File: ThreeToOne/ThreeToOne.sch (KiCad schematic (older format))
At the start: 216 parts, among them SW1 Switch, SW10 Switch, SW100 Switch, SW101 Switch, SW11 Switch, SW12 Switch, SW13 Switch, SW14 Switch, SW15 Switch, SW16 Switch, SW17 REsw, SW18 Switch, SW19 Switch, SW2 Switch, SW20 Switch, SW21 Switch, SW22 Switch, SW23 Switch, SW24 Switch, SW25 Switch, SW26 Switch, SW27 Switch, SW28 Switch, SW29 Switch, SW3 Switch, SW30 Switch, SW31 Switch, SW32 Switch, SW33 Switch, SW34 Switch, SW35 Switch, SW36 Switch, SW37 Switch, SW38 Switch, SW39 Switch, SW4 Switch, SW40 Switch, SW41 Switch, SW42 Switch, SW43 Switch, SW44 Switch, SW45 Switch, SW46 Switch, SW47 Switch, SW48 Switch, SW49 Switch, SW5 Switch, SW50 Switch, SW51 Switch, SW52 Switch, SW53 Switch, SW54 Switch, SW55 Switch, SW56 Switch, SW57 Switch, SW58 Switch, SW59 Switch, SW6 Switch, SW60 Switch, SW61 Switch, SW62 Switch, SW63 Switch, SW64 Switch, SW65 Switch, SW66 Switch, SW67 Switch, SW68 Switch, SW69 Switch, SW7 Switch, SW70 Switch, SW71 Switch, SW72 Switch, SW73 Switch, SW74 Switch, SW75 Switch, SW76 Switch, SW77 Switch, SW78 Switch, SW79 Switch, SW8 Switch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

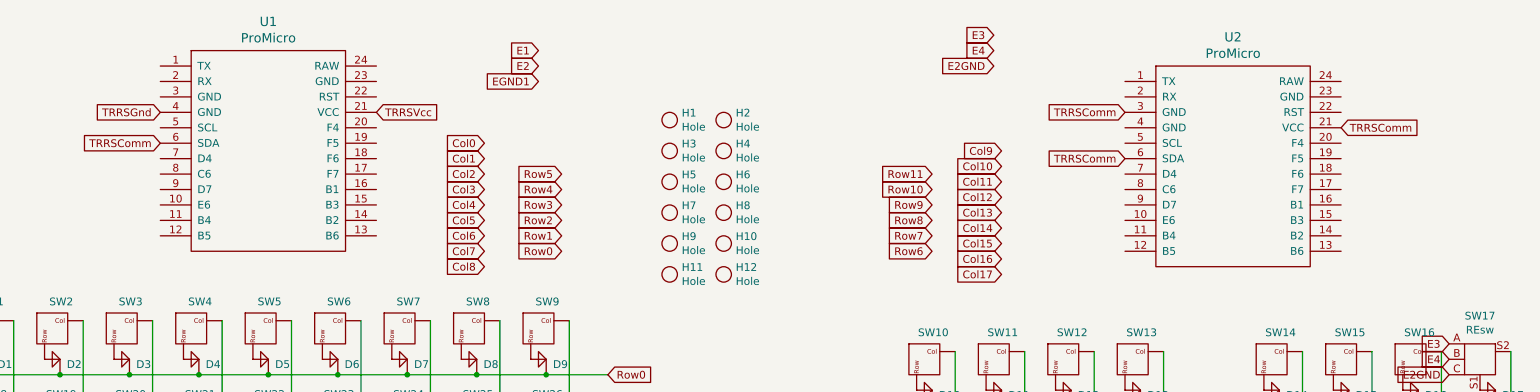
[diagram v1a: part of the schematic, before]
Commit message: Wired all of left half and some of right
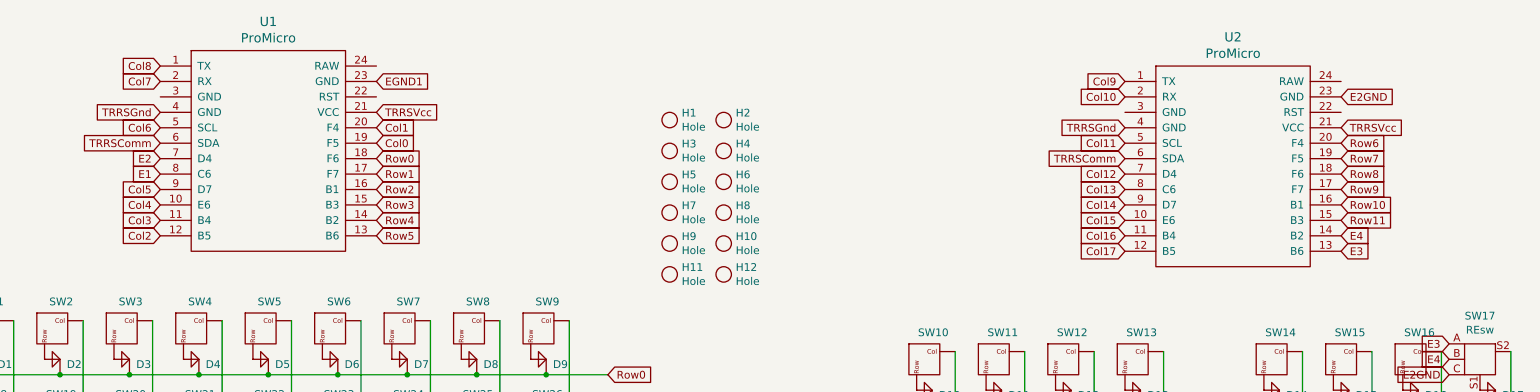
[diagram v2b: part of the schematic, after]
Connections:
- net Col0: now also U1.19 (F5)
- net Col1: now also U1.20 (F4)
- net Col10: now also U2.2 (RX)
- net Col11: now also U2.5 (SCL)
- net Col12: now also U2.7 (D4)
- net Col13: now also U2.8 (C6)
- net Col14: now also U2.9 (D7)
- net Col15: now also U2.10 (E6)
- net Col16: now also U2.11 (B4)
- net Col17: now also U2.12 (B5)
- net Col2: now also U1.12 (B5)
- net Col3: now also U1.11 (B4)
- net Col4: now also U1.10 (E6)
- net Col5: now also U1.9 (D7)
- net Col6: now also U1.5 (SCL)
- net Col7: now also U1.2 (RX)
- net Col8: now also U1.1 (TX)
- net Col9: now also U2.1 (TX)
- net E1: now also U1.8 (C6)
- net E2: now also U1.7 (D4)
- net E2GND: now also U2.23 (GND)
- net E3: now also U2.13 (B6)
- net E4: now also U2.14 (B2)
- net EGND1: now also U1.23 (GND)
- net Row0: now also U1.18 (F6)
- net Row1: now also U1.17 (F7)
- net Row10: now also U2.16 (B1)
- net Row11: now also U2.15 (B3)
- net Row2: now also U1.16 (B1)
- net Row3: now also U1.15 (B3)
- net Row4: now also U1.14 (B2)
- net Row5: now also U1.13 (B6)
- net Row6: now also U2.20 (F4)
- net Row7: now also U2.19 (F5)
- net Row8: now also U2.18 (F6)
- net Row9: now also U2.17 (F7)
- net TRRSComm: no longer U2.21 (VCC), U2.3 (GND)
- net TRRSGnd: now also U2.4 (GND)
- net TRRSVcc: now also U2.21 (VCC)
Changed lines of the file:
@@
 Text GLabel 2000 1100 0    50   Input ~ 0
 TRRSGnd
-Text GLabel 8250 1100 0    50   Input ~ 0
-TRRSComm
 Text GLabel 3400 1100 2    50   Input ~ 0
 TRRSVcc
-Text GLabel 9650 1200 2    50   Input ~ 0
-TRRSComm
-Text GLabel 4450 700  0    50   Input ~ 0
+Text GLabel 2000 1500 0    50   Input ~ 0
 E1
-Text GLabel 4450 800  0    50   Input ~ 0
+Text GLabel 2000 1400 0    50   Input ~ 0
 E2
-Text GLabel 4450 900  0    50   Input ~ 0
+Text GLabel 3400 900  2    50   Input ~ 0
 EGND1
 Connection ~ 4200 5350
@@
 Text GLabel 1050 5900 0    50   Input ~ 0
 Col0
-Text GLabel 4100 1300 0    50   Input ~ 0
+Text GLabel 3400 1300 2    50   Input ~ 0
 Col0
-Text GLabel 4100 1400 0    50   Input ~ 0
+Text GLabel 3400 1200 2    50   Input ~ 0
 Col1
-Text GLabel 4100 1500 0    50   Input ~ 0
+Text GLabel 2000 1900 0    50   Input ~ 0
 Col2
-Text GLabel 4100 1600 0    50   Input ~ 0
+Text GLabel 2000 1800 0    50   Input ~ 0
 Col3
-Text GLabel 4100 1700 0    50   Input ~ 0
+Text GLabel 2000 1700 0    50   Input ~ 0
 Col4
-Text GLabel 4100 1800 0    50   Input ~ 0
+Text GLabel 2000 1600 0    50   Input ~ 0
 Col5
-Text GLabel 4100 1900 0    50   Input ~ 0
+Text GLabel 2000 1200 0    50   Input ~ 0
 Col6
-Text GLabel 4100 2000 0    50   Input ~ 0
+Text GLabel 2000 900  0    50   Input ~ 0
 Col7
-Text GLabel 4100 2100 0    50   Input ~ 0
+Text GLabel 2000 800  0    50   Input ~ 0
 Col8
-Text GLabel 7450 1350 0    50   Input ~ 0
+Text GLabel 8250 900  0    50   Input ~ 0
 Col9
-Text GLabel 7450 1450 0    50   Input ~ 0
+Text GLabel 8250 1000 0    50   Input ~ 0
 Col10
-Text GLabel 7450 1550 0    50   Input ~ 0
+Text GLabel 8250 1300 0    50   Input ~ 0
 Col11
-Text GLabel 7450 1650 0    50   Input ~ 0
+Text GLabel 8250 1500 0    50   Input ~ 0
 Col12
-Text GLabel 7450 1750 0    50   Input ~ 0
+Text GLabel 8250 1600 0    50   Input ~ 0
 Col13
-Text GLabel 7450 1850 0    50   Input ~ 0
+Text GLabel 8250 1700 0    50   Input ~ 0
 Col14
-Text GLabel 7450 1950 0    50   Input ~ 0
+Text GLabel 8250 1800 0    50   Input ~ 0
 Col15
-Text GLabel 7450 2050 0    50   Input ~ 0
+Text GLabel 8250 1900 0    50   Input ~ 0
 Col16
-Text GLabel 7450 2150 0    50   Input ~ 0
+Text GLabel 8250 2000 0    50   Input ~ 0
 Col17
 Text GLabel 6600 5900 0    50   Input ~ 0
@@
 Text GLabel 6600 3000 0    50   Input ~ 0
 Row6
-Text GLabel 4600 2000 0    50   Input ~ 0
+Text GLabel 3400 1400 2    50   Input ~ 0
 Row0
-Text GLabel 4600 1900 0    50   Input ~ 0
+Text GLabel 3400 1500 2    50   Input ~ 0
 Row1
-Text GLabel 4600 1800 0    50   Input ~ 0
+Text GLabel 3400 1600 2    50   Input ~ 0
 Row2
-Text GLabel 4600 1700 0    50   Input ~ 0
+Text GLabel 3400 1700 2    50   Input ~ 0
 Row3
-Text GLabel 4600 1500 0    50   Input ~ 0
+Text GLabel 3400 1900 2    50   Input ~ 0
 Row5
-Text GLabel 4600 1600 0    50   Input ~ 0
+Text GLabel 3400 1800 2    50   Input ~ 0
 Row4
-Text GLabel 7000 1500 0    50   Input ~ 0
+Text GLabel 9650 1800 2    50   Input ~ 0
 Row11
-Text GLabel 7000 1600 0    50   Input ~ 0
+Text GLabel 9650 1700 2    50   Input ~ 0
 Row10
-Text GLabel 7000 1700 0    50   Input ~ 0
+Text GLabel 9650 1600 2    50   Input ~ 0
 Row9
-Text GLabel 7000 1800 0    50   Input ~ 0
+Text GLabel 9650 1500 2    50   Input ~ 0
 Row8
-Text GLabel 7000 1900 0    50   Input ~ 0
+Text GLabel 9650 1400 2    50   Input ~ 0
 Row7
-Text GLabel 7000 2000 0    50   Input ~ 0
+Text GLabel 9650 1300 2    50   Input ~ 0
 Row6
-Text GLabel 7400 600  0    50   Input ~ 0
+Text GLabel 9650 2000 2    50   Input ~ 0
 E3
-Text GLabel 7400 700  0    50   Input ~ 0
+Text GLabel 9650 1900 2    50   Input ~ 0
 E4
-Text GLabel 7400 800  0    50   Input ~ 0
+Text GLabel 9650 1000 2    50   Input ~ 0
 E2GND
 $Comp
@@
 	1    0    0    -1
 $EndComp
+Text GLabel 8250 1200 0    50   Input ~ 0
+TRRSGnd
+Text GLabel 9650 1200 2    50   Input ~ 0
+TRRSVcc
 $EndSCHEMATC

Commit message: Finished + gerbers
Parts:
- removed H1, H10, H11, H12, H2, H3, H4, H5, H6, H7, H8, H9: Hole, KeyboardFootprints:Hole_2mm, symbol KeyboardLibrary:Hole
- removed U2: ProMicro, KeyboardFootprints:ProMicro, symbol KeyboardLibrary:ProMicro
- added LED0, LED1: Diode, KeyboardFootprints:Diode, symbol KeyboardLibrary:Diode
- added R0, R1: Resistor, KeyboardFootprints:Resistor, symbol KeyboardLibrary:Resistor
- added U2: Elite-C, Keebio-Parts:Elite-C, symbol keebio:Elite-C
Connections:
- net Col10: now also U2.2 (RX1/PD2)
- net Col11: now also U2.5 (2/PD1)
- net Col12: now also U2.7 (4/PD4)
- net Col13: now also U2.8 (5/PC6)
- net Col14: now also U2.9 (6/PD7)
- net Col15: now also U2.10 (7/PE6)
- net Col16: now also U2.11 (8/PB4)
- net Col17: now also U2.12 (9/PB5)
- net Col9: now also U2.1 (TX0/PD3)
- net E2GND: now also R0.1, R1.1, U2.23 (GND)
- net E3: now also U2.25 (B7)
- net E4: now also U2.26 (D5)
- net Row10: now also U2.17 (A0/PF7)
- net Row11: now also U2.18 (A1/PF6)
- net Row6: now also U2.20 (A3/PF4)
- net Row7: now also U2.19 (A2/PF5)
- net Row8: now also U2.15 (14/PB3)
- net Row9: now also U2.16 (15/PB1)
- net TRRSComm: now also U2.6 (3/PD0)
- net TRRSGnd: now also U2.4 (GND)
- net TRRSVcc: now also U2.21 (VCC)
- new net: LED1.1 (K), U2.13 (10/PB6)
- new net: LED0.1 (K), U2.14 (16/PB2)
- new net: LED0.2 (A), R0.2
- new net: LED1.2 (A), R1.2
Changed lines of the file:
@@
-	1    0    0    -1
-$EndComp
-$Comp
-L KeyboardLibrary:ProMicro U2
-U 1 1 607B0D82
-P 8950 1650
-F 0 "U2" H 8950 2687 60  0000 C CNN
-F 1 "ProMicro" H 8950 2581 60  0000 C CNN
-F 2 "KeyboardFootprints:ProMicro" H 9050 600 60  0001 C CNN
-F 3 "" H 9050 600 60  0000 C CNN
-	1    8950 1650
 	1    0    0    -1
 $EndComp
@@
 Text GLabel 10350 2800 0    50   Input ~ 0
 E2GND
-Text GLabel 8250 1400 0    50   Input ~ 0
+Text GLabel 8200 1400 0    50   Input ~ 0
 TRRSComm
 Text GLabel 2000 1300 0    50   Input ~ 0
@@
 Text GLabel 2000 800  0    50   Input ~ 0
 Col8
-Text GLabel 8250 900  0    50   Input ~ 0
+Text GLabel 8200 900  0    50   Input ~ 0
 Col9
-Text GLabel 8250 1000 0    50   Input ~ 0
+Text GLabel 8200 1000 0    50   Input ~ 0
 Col10
-Text GLabel 8250 1300 0    50   Input ~ 0
+Text GLabel 8200 1300 0    50   Input ~ 0
 Col11
-Text GLabel 8250 1500 0    50   Input ~ 0
+Text GLabel 8200 1500 0    50   Input ~ 0
 Col12
-Text GLabel 8250 1600 0    50   Input ~ 0
+Text GLabel 8200 1600 0    50   Input ~ 0
 Col13
-Text GLabel 8250 1700 0    50   Input ~ 0
+Text GLabel 8200 1700 0    50   Input ~ 0
 Col14
-Text GLabel 8250 1800 0    50   Input ~ 0
+Text GLabel 8200 1800 0    50   Input ~ 0
 Col15
-Text GLabel 8250 1900 0    50   Input ~ 0
+Text GLabel 8200 1900 0    50   Input ~ 0
 Col16
-Text GLabel 8250 2000 0    50   Input ~ 0
+Text GLabel 8200 2000 0    50   Input ~ 0
 Col17
 Text GLabel 6600 5900 0    50   Input ~ 0
@@
 Text GLabel 3400 1800 2    50   Input ~ 0
 Row4
-Text GLabel 9650 1800 2    50   Input ~ 0
-Row11
-Text GLabel 9650 1700 2    50   Input ~ 0
-Row10
-Text GLabel 9650 1600 2    50   Input ~ 0
-Row9
-Text GLabel 9650 1500 2    50   Input ~ 0
-Row8
-Text GLabel 9650 1400 2    50   Input ~ 0
-Row7
-Text GLabel 9650 1300 2    50   Input ~ 0
-Row6
-Text GLabel 9650 2000 2    50   Input ~ 0
+Text GLabel 8700 2400 3    50   Input ~ 0
 E3
-Text GLabel 9650 1900 2    50   Input ~ 0
+Text GLabel 8800 2400 3    50   Input ~ 0
 E4
-Text GLabel 9650 1000 2    50   Input ~ 0
-E2GND
-$Comp
-L KeyboardLibrary:Hole H1
-U 1 1 604DCAA4
-P 5300 1150
-F 0 "H1" H 5378 1196 50  0000 L CNN
-F 1 "Hole" H 5378 1105 50  0000 L CNN
-F 2 "KeyboardFootprints:Hole_2mm" H 5300 1100 50  0001 C CNN
-F 3 "" H 5300 1100 50  0001 C CNN
-	1    5300 1150
-	1    0    0    -1
-$EndComp
-$Comp
-L KeyboardLibrary:Hole H3
-U 1 1 604DF4A1
-P 5300 1350
-F 0 "H3" H 5378 1396 50  0000 L CNN
-F 1 "Hole" H 5378 1305 50  0000 L CNN
-F 2 "KeyboardFootprints:Hole_2mm" H 5300 1300 50  0001 C CNN
-F 3 "" H 5300 1300 50  0001 C CNN
-	1    5300 1350
-	1    0    0    -1
-$EndComp
-$Comp
-L KeyboardLibrary:Hole H5
-U 1 1 604EAA4A
-P 5300 1550
-F 0 "H5" H 5378 1596 50  0000 L CNN
-F 1 "Hole" H 5378 1505 50  0000 L CNN
-F 2 "KeyboardFootprints:Hole_2mm" H 5300 1500 50  0001 C CNN
-F 3 "" H 5300 1500 50  0001 C CNN
-	1    5300 1550
-	1    0    0    -1
-$EndComp
-$Comp
-L KeyboardLibrary:Hole H2
-U 1 1 604F6F10
-P 5650 1150
-F 0 "H2" H 5728 1196 50  0000 L CNN
-F 1 "Hole" H 5728 1105 50  0000 L CNN
-F 2 "KeyboardFootprints:Hole_2mm" H 5650 1100 50  0001 C CNN
-F 3 "" H 5650 1100 50  0001 C CNN
-	1    5650 1150
-	1    0    0    -1
-$EndComp
-$Comp
-L KeyboardLibrary:Hole H4
-U 1 1 604F6F16
-P 5650 1350
-F 0 "H4" H 5728 1396 50  0000 L CNN
-F 1 "Hole" H 5728 1305 50  0000 L CNN
-F 2 "KeyboardFootprints:Hole_2mm" H 5650 1300 50  0001 C CNN
-F 3 "" H 5650 1300 50  0001 C CNN
-	1    5650 1350
-	1    0    0    -1
-$EndComp
-$Comp
-L KeyboardLibrary:Hole H6
-U 1 1 604F6F1C
-P 5650 1550
-F 0 "H6" H 5728 1596 50  0000 L CNN
-F 1 "Hole" H 5728 1505 50  0000 L CNN
-F 2 "KeyboardFootprints:Hole_2mm" H 5650 1500 50  0001 C CNN
-F 3 "" H 5650 1500 50  0001 C CNN
-	1    5650 1550
-	1    0    0    -1
-$EndComp
-$Comp
-L KeyboardLibrary:Hole H8
-U 1 1 60502740
-P 5650 1750
-F 0 "H8" H 5728 1796 50  0000 L CNN
-F 1 "Hole" H 5728 1705 50  0000 L CNN
-F 2 "KeyboardFootprints:Hole_2mm" H 5650 1700 50  0001 C CNN
-F 3 "" H 5650 1700 50  0001 C CNN
-	1    5650 1750
-	1    0    0    -1
-$EndComp
-$Comp
-L KeyboardLibrary:Hole H10
-U 1 1 60502746
-P 5650 1950
-F 0 "H10" H 5728 1996 50  0000 L CNN
-F 1 "Hole" H 5728 1905 50  0000 L CNN
-F 2 "KeyboardFootprints:Hole_2mm" H 5650 1900 50  0001 C CNN
-F 3 "" H 5650 1900 50  0001 C CNN
-	1    5650 1950
-	1    0    0    -1
-$EndComp
-$Comp
-L KeyboardLibrary:Hole H12
-U 1 1 6050274C
-P 5650 2150
-F 0 "H12" H 5728 2196 50  0000 L CNN
-F 1 "Hole" H 5728 2105 50  0000 L CNN
-F 2 "KeyboardFootprints:Hole_2mm" H 5650 2100 50  0001 C CNN
-F 3 "" H 5650 2100 50  0001 C CNN
-	1    5650 2150
-	1    0    0    -1
-$EndComp
-$Comp
-L KeyboardLibrary:Hole H7
-U 1 1 6050DD66
-P 5300 1750
-F 0 "H7" H 5378 1796 50  0000 L CNN
-F 1 "Hole" H 5378 1705 50  0000 L CNN
-F 2 "KeyboardFootprints:Hole_2mm" H 5300 1700 50  0001 C CNN
-F 3 "" H 5300 1700 50  0001 C CNN
-	1    5300 1750
-	1    0    0    -1
-$EndComp
-$Comp
-L KeyboardLibrary:Hole H9
-U 1 1 6050DD6C
-P 5300 1950
-F 0 "H9" H 5378 1996 50  0000 L CNN
-F 1 "Hole" H 5378 1905 50  0000 L CNN
-F 2 "KeyboardFootprints:Hole_2mm" H 5300 1900 50  0001 C CNN
-F 3 "" H 5300 1900 50  0001 C CNN
-	1    5300 1950
-	1    0    0    -1
-$EndComp
-$Comp
-L KeyboardLibrary:Hole H11
-U 1 1 6050DD72
-P 5300 2150
-F 0 "H11" H 5378 2196 50  0000 L CNN
-F 1 "Hole" H 5378 2105 50  0000 L CNN
-F 2 "KeyboardFootprints:Hole_2mm" H 5300 2100 50  0001 C CNN
-F 3 "" H 5300 2100 50  0001 C CNN
-	1    5300 2150
-	1    0    0    -1
-$EndComp
 Wire Wire Line
 	2250 3950 2700 3950
@@
 	1    0    0    -1
 $EndComp
-Text GLabel 8250 1200 0    50   Input ~ 0
+Text GLabel 8200 1200 0    50   Input ~ 0
 TRRSGnd
-Text GLabel 9650 1200 2    50   Input ~ 0
+$Comp
+L keebio:Elite-C U2
+U 1 1 6055E9BB
+P 8900 1450
+F 0 "U2" H 8900 2287 60  0000 C CNN
+F 1 "Elite-C" H 8900 2181 60  0000 C CNN
+F 2 "Keebio-Parts:Elite-C" V 9950 -1050 60  0001 C CNN
+F 3 "" V 9950 -1050 60  0001 C CNN
+	1    8900 1450
+	1    0    0    -1
+$EndComp
+Text GLabel 9600 1200 2    50   Input ~ 0
 TRRSVcc
+Text GLabel 9850 1000 2    50   Input ~ 0
+E2GND
+Text GLabel 9600 1300 2    50   Input ~ 0
+Row6
+Text GLabel 9600 1400 2    50   Input ~ 0
+Row7
+Text GLabel 9600 1800 2    50   Input ~ 0
+Row8
+Text GLabel 9600 1700 2    50   Input ~ 0
+Row9
+Text GLabel 9600 1600 2    50   Input ~ 0
+Row10
+Text GLabel 9600 1500 2    50   Input ~ 0
+Row11
+$Comp
+L KeyboardLibrary:Diode LED0
+U 1 1 606358A6
+P 9800 1900
+F 0 "LED0" H 9944 1867 50  0000 L CNN
+F 1 "Diode" H 9900 2000 50  0001 C CNN
+F 2 "KeyboardFootprints:Diode" H 9900 2000 50  0001 C CNN
+F 3 "" H 9900 2000 50  0001 C CNN
+	1    9800 1900
+	1    0    0    -1
+$EndComp
+$Comp
+L KeyboardLibrary:Diode LED1
+U 1 1 60637F62
+P 9600 2000
+F 0 "LED1" H 9744 1967 50  0000 L CNN
+F 1 "Diode" H 9700 2100 50  0001 C CNN
+F 2 "KeyboardFootprints:Diode" H 9700 2100 50  0001 C CNN
+F 3 "" H 9700 2100 50  0001 C CNN
+	1    9600 2000
+	1    0    0    -1
+$EndComp
+Wire Wire Line
+	9600 1900 9800 1900
+Wire Wire Line
+	9800 1000 9800 1100
+Wire Wire Line
+	9800 1100 10200 1100
+Wire Wire Line
+	9600 1000 9800 1000
+Connection ~ 9800 1000
+Wire Wire Line
+	9800 1000 9850 1000
+$Comp
+L KeyboardLibrary:Resistor R0
+U 1 1 6065EAE1
+P 10050 2000
+F 0 "R0" H 10050 1877 50  0000 C CNN
+F 1 "Resistor" H 10050 2000 50  0001 C CNN
+F 2 "KeyboardFootprints:Resistor" H 10050 2000 50  0001 C CNN
+F 3 "" H 10050 2000 50  0001 C CNN
+	1    10050 2000
+	-1   0    0    1
+$EndComp
+$Comp
+L KeyboardLibrary:Resistor R1
+U 1 1 6067AA95
+P 9850 2100
+F 0 "R1" H 9850 1977 50  0000 C CNN
+F 1 "Resistor" H 9850 2100 50  0001 C CNN
+F 2 "KeyboardFootprints:Resistor" H 9850 2100 50  0001 C CNN
+F 3 "" H 9850 2100 50  0001 C CNN
+	1    9850 2100
+	-1   0    0    1
+$EndComp
+Wire Wire Line
+	10000 2100 10200 2100
+Wire Wire Line
+	10200 2100 10200 2000
+Wire Wire Line
+	10200 2000 10200 1100
+Connection ~ 10200 2000
 $EndSCHEMATC

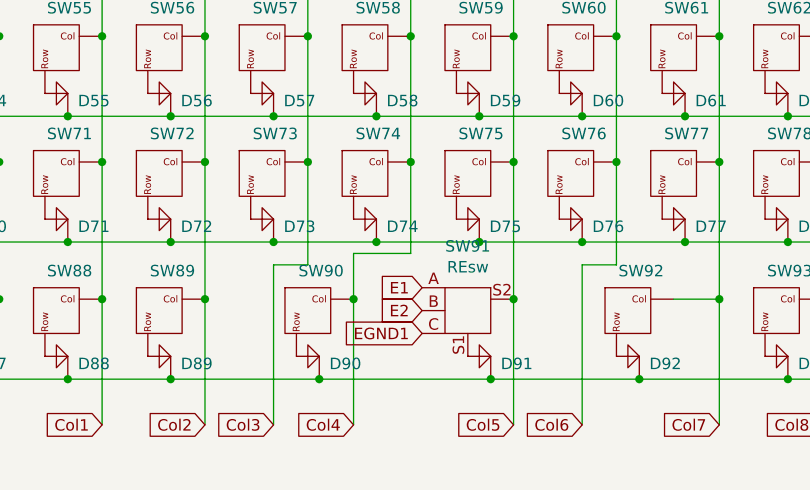
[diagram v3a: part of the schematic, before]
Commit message: moved enc to the left
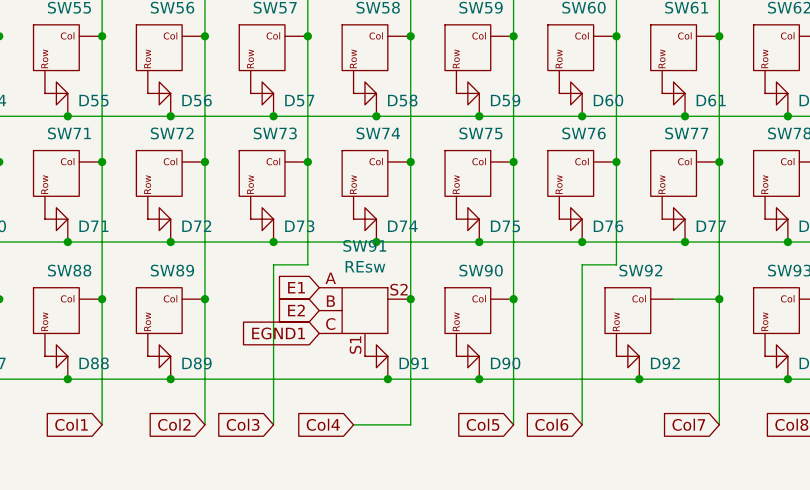
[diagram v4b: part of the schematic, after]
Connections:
- net Col4: now also SW91.S2; no longer SW90.1
- net Col5: now also SW90.1; no longer SW91.S2
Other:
- moved on the sheet: D90, D91, SW90, SW91
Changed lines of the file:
@@
 L KeyboardLibrary:Switch SW90
 U 1 1 60535E84
-P 2500 5500
-F 0 "SW90" H 2458 5773 50  0000 C CNN
-F 1 "Switch" H 2450 5550 50  0001 C CNN
-F 2 "KeyboardFootprints:MX_Choc_Symmetric" H 2500 5500 50  0001 C CNN
-F 3 "" H 2500 5500 50  0001 C CNN
-	1    2500 5500
+P 3200 5500
+F 0 "SW90" H 3158 5773 50  0000 C CNN
+F 1 "Switch" H 3150 5550 50  0001 C CNN
+F 2 "KeyboardFootprints:MX_Choc_Symmetric" H 3200 5500 50  0001 C CNN
+F 3 "" H 3200 5500 50  0001 C CNN
+	1    3200 5500
 	1    0    0    -1
 $EndComp
@@
 L KeyboardLibrary:Diode D90
 U 1 1 60535E7E
-P 2350 5600
-F 0 "D90" H 2494 5567 50  0000 L CNN
-F 1 "Diode" H 2450 5700 50  0001 C CNN
-F 2 "KeyboardFootprints:Diode" H 2450 5700 50  0001 C CNN
-F 3 "" H 2450 5700 50  0001 C CNN
-	1    2350 5600
+P 3050 5600
+F 0 "D90" H 3194 5567 50  0000 L CNN
+F 1 "Diode" H 3150 5700 50  0001 C CNN
+F 2 "KeyboardFootprints:Diode" H 3150 5700 50  0001 C CNN
+F 3 "" H 3150 5700 50  0001 C CNN
+	1    3050 5600
 	1    0    0    -1
 $EndComp
@@
 L KeyboardLibrary:REsw SW91
 U 1 1 60760716
-P 3100 5450
-F 0 "SW91" H 3100 5781 50  0000 C CNN
-F 1 "REsw" H 3100 5690 50  0000 C CNN
-F 2 "KeyboardFootprints:REsw" H 2600 5910 50  0001 C CNN
-F 3 "~" V 3260 5600 50  0001 C CNN
-	1    3100 5450
+P 2650 5450
+F 0 "SW91" H 2650 5781 50  0000 C CNN
+F 1 "REsw" H 2650 5690 50  0000 C CNN
+F 2 "KeyboardFootprints:REsw" H 2150 5910 50  0001 C CNN
+F 3 "~" V 2810 5600 50  0001 C CNN
+	1    2650 5450
 	1    0    0    -1
 $EndComp
@@
 L KeyboardLibrary:Diode D91
 U 1 1 60535EBA
-P 3100 5600
-F 0 "D91" H 3244 5567 50  0000 L CNN
-F 1 "Diode" H 3200 5700 50  0001 C CNN
-F 2 "KeyboardFootprints:Diode" H 3200 5700 50  0001 C CNN
-F 3 "" H 3200 5700 50  0001 C CNN
-	1    3100 5600
+P 2650 5600
+F 0 "D91" H 2794 5567 50  0000 L CNN
+F 1 "Diode" H 2750 5700 50  0001 C CNN
+F 2 "KeyboardFootprints:Diode" H 2750 5700 50  0001 C CNN
+F 3 "" H 2750 5700 50  0001 C CNN
+	1    2650 5600
 	1    0    0    -1
 $EndComp
@@
 	1350 5700 1800 5700
 Connection ~ 1800 5700
-Wire Wire Line
-	1800 5700 2450 5700
-Connection ~ 2450 5700
-Wire Wire Line
-	2450 5700 3200 5700
 Connection ~ 3850 5700
 Wire Wire Line
@@
 Wire Wire Line
 	4650 4750 4650 4200
-Connection ~ 3200 5700
-Wire Wire Line
-	3200 5700 3850 5700
-Wire Wire Line
-	3300 5350 3300 4750
-Wire Wire Line
-	2600 5350 2600 5150
-Wire Wire Line
-	2600 5150 2850 5150
-Wire Wire Line
-	2850 5150 2850 4750
-Text GLabel 2900 5300 0    50   Input ~ 0
+Text GLabel 2450 5300 0    50   Input ~ 0
 E1
-Text GLabel 2900 5400 0    50   Input ~ 0
+Text GLabel 2450 5400 0    50   Input ~ 0
 E2
-Text GLabel 2900 5500 0    50   Input ~ 0
+Text GLabel 2450 5500 0    50   Input ~ 0
 EGND1
 Connection ~ 7000 3000
@@
 EGND1
 Connection ~ 4200 5350
-Connection ~ 3300 5350
-Connection ~ 2600 5350
 Connection ~ 1950 5350
 Connection ~ 1500 5350
@@
 Wire Wire Line
 	4200 5350 4200 5900
-Wire Wire Line
-	3300 5350 3300 5900
-Wire Wire Line
-	2600 5350 2600 5900
 Wire Wire Line
 	2250 5200 2250 5900
@@
 	10200 2000 10200 1100
 Connection ~ 10200 2000
+Wire Wire Line
+	3300 4750 3300 5350
+Wire Wire Line
+	1800 5700 2750 5700
+Connection ~ 2750 5700
+Wire Wire Line
+	2750 5700 3150 5700
+Wire Wire Line
+	2850 5900 2600 5900
+Wire Wire Line
+	2850 4750 2850 5350
+Connection ~ 2850 5350
+Wire Wire Line
+	2850 5350 2850 5900
+Connection ~ 3150 5700
+Wire Wire Line
+	3150 5700 3850 5700
+Connection ~ 3300 5350
+Wire Wire Line
+	3300 5350 3300 5900
 $EndSCHEMATC
